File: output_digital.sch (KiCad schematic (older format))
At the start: 18 parts

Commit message: Primer version
Esquematico completo, faltan notas del revisor.
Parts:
- removed D? (x2): LED_ALT, symbol LED_ALT
- removed D?: DIODE, symbol DIODE
- removed J? (x2): Screw_Terminal_1x02, symbol Screw_Terminal_1x02
- removed K? (x4): RELAY-DPDT-EE2-SPLIT, symbol RELAY-DPDT-EE2-SPLIT
- removed Q? (x2): BT3904, TO_SOT_Packages_SMD:SOT-23, symbol MBT3904DW1
- removed R? (x3): 1k, symbol R
- removed R? (x2): 10k, symbol R
- added D1, D2, D5: LED_ALT, footprints:LED-0805, symbol LED_ALT
- added D4: MRA4003T3G, footprints:DO-214AA(SMB), symbol DIODE
- added J4, J5, J6: Screw_Terminal_1x02, footprints:TerminalBlock_Pheonix_MKDS1.5-2pol, symbol Screw_Terminal_1x02
- added Q1, Q2: MMBT3904, footprints:SOT23GDS, symbol MMBT3904
- added R3, R4, R5, R6: 1k, footprints:R_1206_HandSoldering, symbol R
- added R7, R8: 10k, footprints:R_1206_HandSoldering, symbol R
- added R9: 100, footprints:R_1206_HandSoldering, symbol R
- added U5, U6: G2RL-1A-E, footprints:Relay_SPST_Schrack-RP-II-1_RM3-5mm, symbol G5LE-1A-5DC
- D3: renamed from D?; value DIODE -> MRA4003T3G; footprint (none) -> footprints:DO-214AA(SMB); Description (none) -> Diode Standard 300V 1A SMA; Digikey# (none) -> MRA4003T3GOSTR-ND; Manf (none) -> ON Semiconductor; Manf# (none) -> MRA4003T3G; Mouser# (none) -> Value
- R2: renamed from R?; footprint (none) -> footprints:R_1206_HandSoldering; Description (none) -> 1k Ohm ±1% 0.25W, 1/4W Chip Resistor 1206 (3216 Metric) Moi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; Digikey# Value -> 311-1.00KFRTR-ND; Manf Value -> Yageo; Manf# Value -> RC1206FR-071KL; Mouser# (none) -> Value
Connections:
- net labels added: REL1_SEL, REL2_SEL, SSR_SEL
- wire segments 34 -> 39
- no-connect marks 2 -> 0
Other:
- note added: "Salida SSR (Solid State Realy)"
- note added: "Salidas a Relay - 16A - 440VAC, 300VDC"
- moved on the sheet: D3, R2

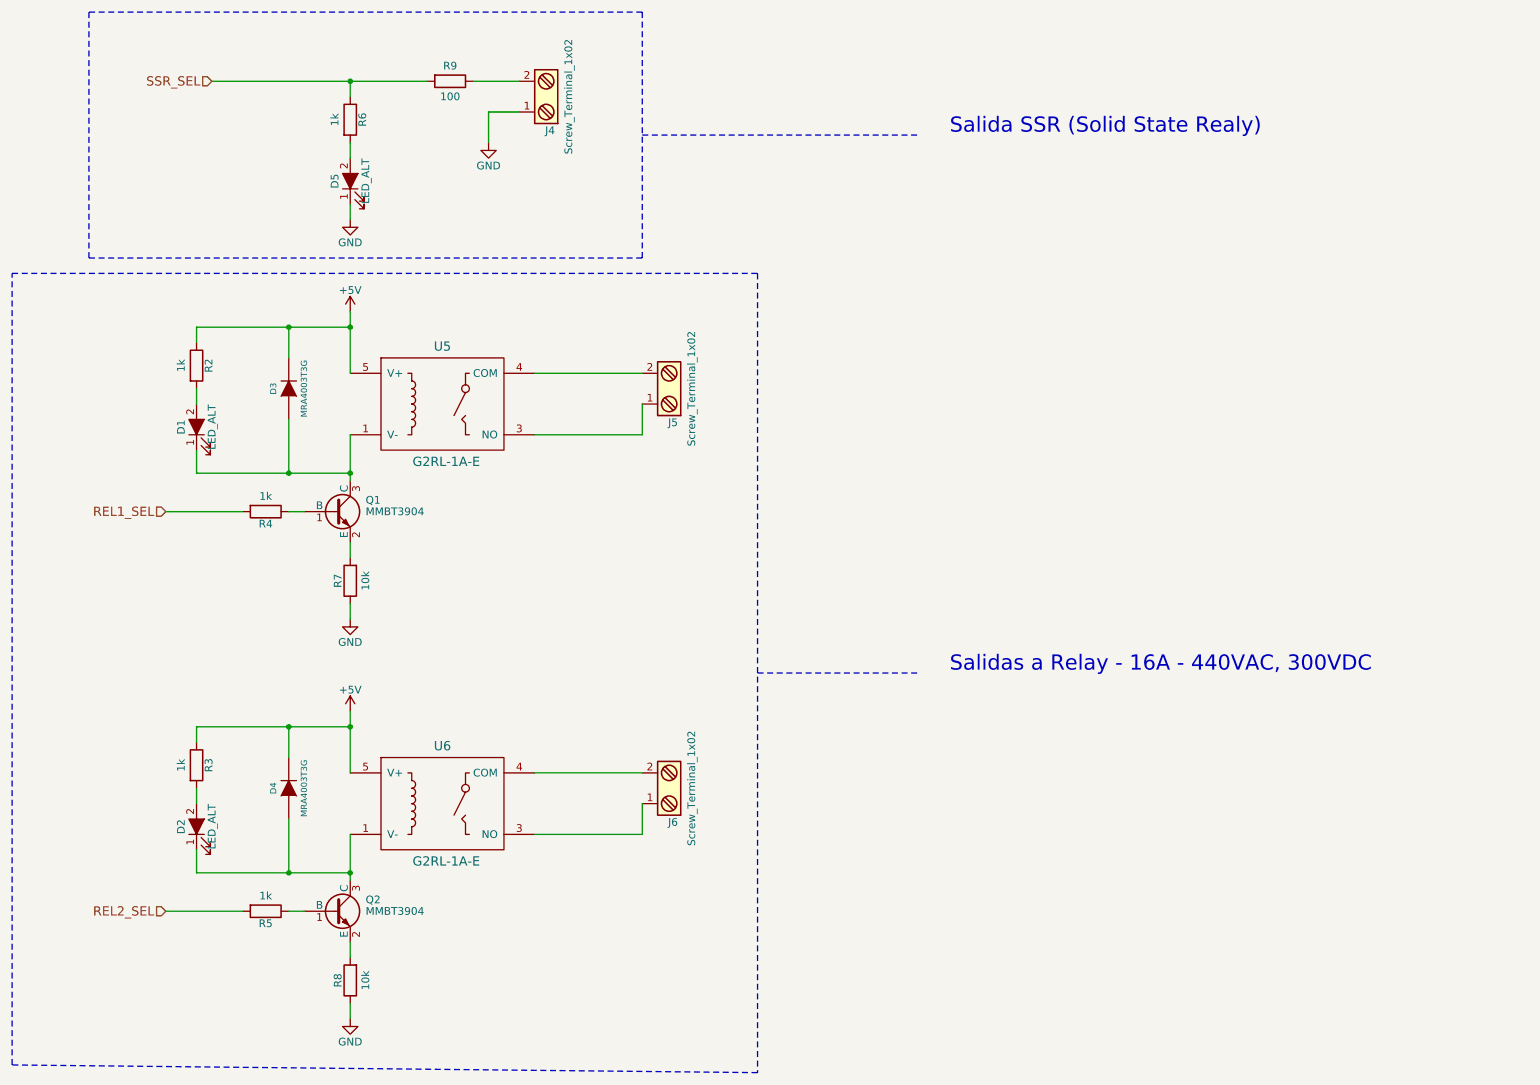
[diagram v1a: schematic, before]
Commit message: Primer revision
Se agregar correcciones del revisor. Se modifica entrada termocupla.
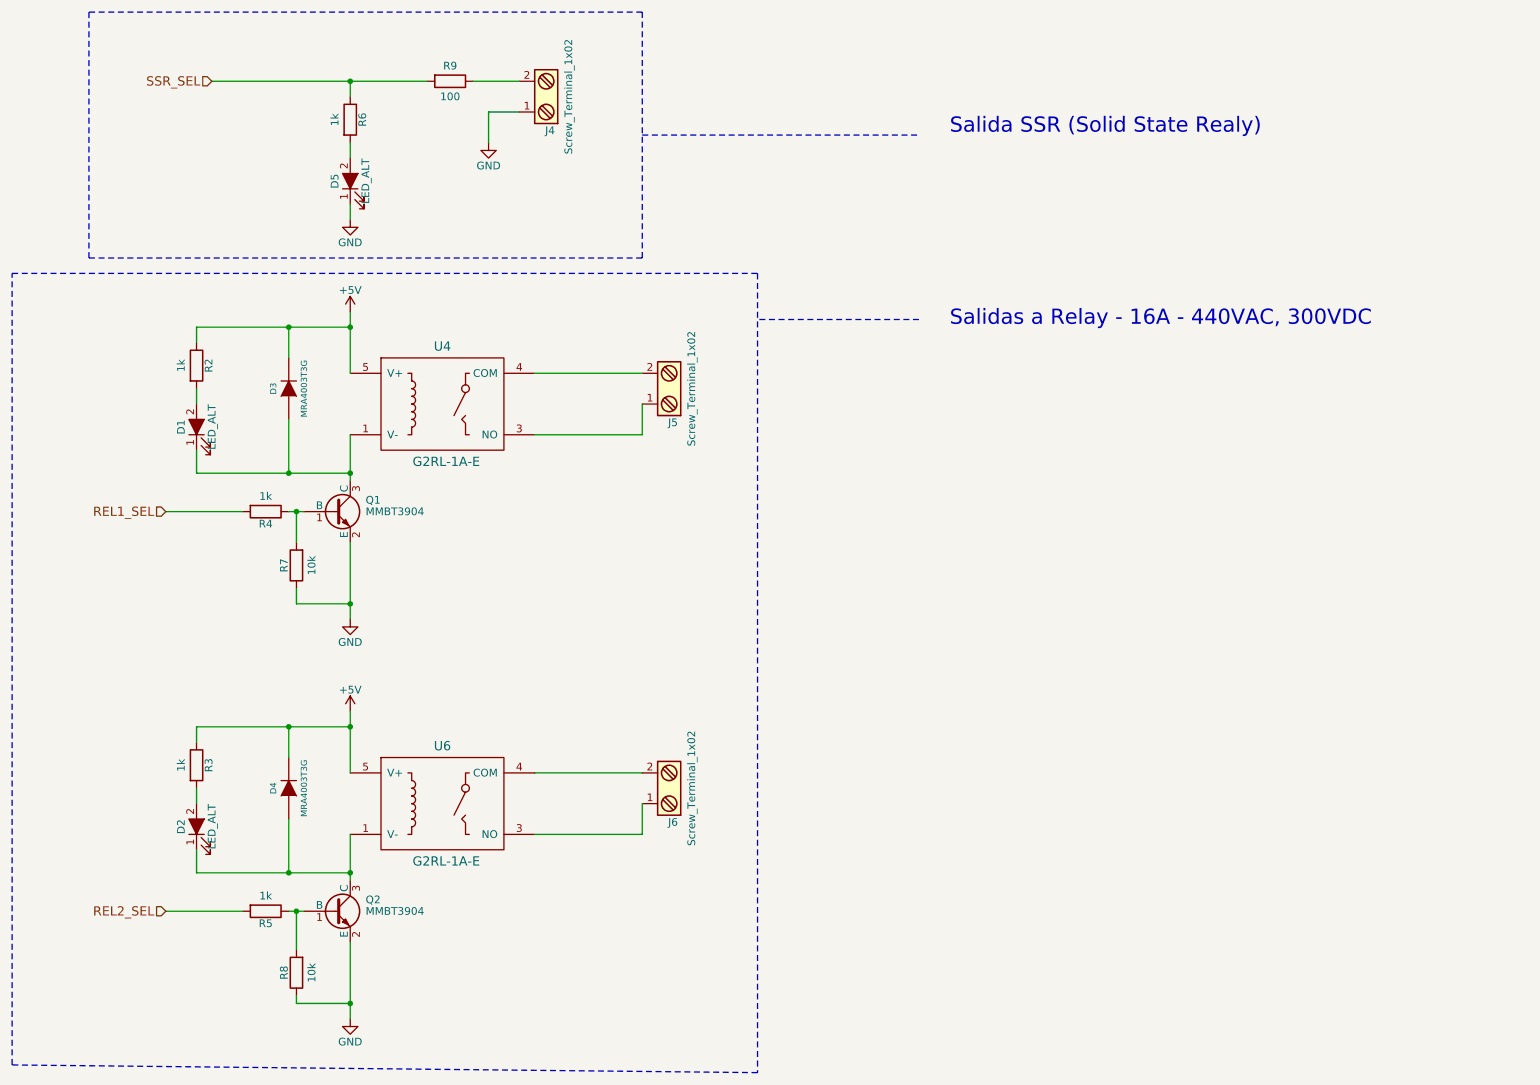
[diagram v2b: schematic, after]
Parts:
- removed U5: G2RL-1A-E, footprints:Relay_SPST_Schrack-RP-II-1_RM3-5mm, symbol G5LE-1A-5DC
- added U4: G2RL-1A-E, footprints:Relay_SPST_Schrack-RP-II-1_RM3-5mm, symbol G5LE-1A-5DC
- U6: Description General Purpose Relays 1 form A w/ TV3 24VDC Coil, 16A -> General Purpose Relays 1 form A w/ TV3 5VDC Coil, 16A; Manf# G2RL-1A-E-ASI DC24 -> G2RL-1A-E-ASI DC5; Mouser# 653-G2RL1AEASIDC24 -> 653-G2RL1AEASIDC5
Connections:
- net +5V: now also U4.5 (V+)
- net GND: now also Q1.2 (E), Q2.2 (E)
- net at D1.1 (K), D3.1 (A), Q1.3 (C): now also U4.1 (V-)
- net at Q1.1 (B), R4.1: now also R7.2
- net at J5.1: now also U4.3 (NO)
- net at J5.2: now also U4.4 (COM)
- net at Q2.1 (B), R5.1: now also R8.2
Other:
- moved on the sheet: R7, R8
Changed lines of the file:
@@
 EESchema Schematic File Version 2
-LIBS:tempRalayPoncho-rescue
-LIBS:power
-LIBS:device
-LIBS:transistors
-LIBS:conn
-LIBS:linear
-LIBS:regul
-LIBS:74xx
-LIBS:cmos4000
-LIBS:adc-dac
-LIBS:memory
-LIBS:xilinx
-LIBS:microcontrollers
-LIBS:dsp
-LIBS:microchip
-LIBS:analog_switches
-LIBS:motorola
-LIBS:texas
-LIBS:intel
-LIBS:audio
-LIBS:interface
-LIBS:digital-audio
-LIBS:philips
-LIBS:display
-LIBS:cypress
-LIBS:siliconi
-LIBS:opto
-LIBS:atmel
-LIBS:contrib
-LIBS:valves
-LIBS:ej2cese
-LIBS:analog-cache
-LIBS:ciaa-nxp-cache
-LIBS:relay
-LIBS:cmos_ieee
-LIBS:tempRalayPoncho-cache
+LIBS:TempRelay
+LIBS:tempRelayPoncho-cache
 EELAYER 25 0
 EELAYER END
@@
 encoding utf-8
 Sheet 4 4
-Title "Poncho Edu CIAA - Sensor Temperatura y Salidas digitales"
+Title "Poncho Edu CIAA - Salidas digitales"
 Date "2017-06-14"
 Rev "1.0"
-Comp "Autor: Francisco Suarez"
+Comp "Autor: Francisco Suárez"
 Comment1 "Revisor:  Mariano Orlante"
 Comment2 "Licencia: 'Docs/Licencia.txt\""
@@
 $EndComp
 $Comp
-L +5V #PWR018
+L +5V #PWR15
 U 1 1 5949AA7B
 P 3900 2550
-F 0 "#PWR018" H 3900 2400 50  0001 C CNN
+F 0 "#PWR15" H 3900 2400 50  0001 C CNN
 F 1 "+5V" H 3900 2690 50  0000 C CNN
 F 2 "" H 3900 2550 50  0001 C CNN
@@
 $EndComp
 $Comp
-L GND #PWR019
+L GND #PWR16
 U 1 1 5949AA9F
 P 3900 4550
-F 0 "#PWR019" H 3900 4300 50  0001 C CNN
+F 0 "#PWR16" H 3900 4300 50  0001 C CNN
 F 1 "GND" H 3900 4400 50  0000 C CNN
 F 2 "" H 3900 4550 50  0001 C CNN
@@
 	3600 3850 3500 3850
 Wire Wire Line
-	3900 4050 3900 4150
-Wire Wire Line
-	3900 4450 3900 4550
+	3900 4050 3900 4550
 Wire Wire Line
 	3200 3850 2700 3850
@@
 	5100 2950 5800 2950
 $Comp
-L +5V #PWR020
+L +5V #PWR17
 U 1 1 594AF973
 P 3900 5150
-F 0 "#PWR020" H 3900 5000 50  0001 C CNN
+F 0 "#PWR17" H 3900 5000 50  0001 C CNN
 F 1 "+5V" H 3900 5290 50  0000 C CNN
 F 2 "" H 3900 5150 50  0001 C CNN
@@
 $EndComp
 $Comp
-L GND #PWR021
+L GND #PWR18
 U 1 1 594AF979
 P 3900 7150
-F 0 "#PWR021" H 3900 6900 50  0001 C CNN
+F 0 "#PWR18" H 3900 6900 50  0001 C CNN
 F 1 "GND" H 3900 7000 50  0000 C CNN
 F 2 "" H 3900 7150 50  0001 C CNN
@@
 	3600 6450 3500 6450
 Wire Wire Line
-	3900 6650 3900 6750
-Wire Wire Line
-	3900 7050 3900 7150
+	3900 6650 3900 7150
 Wire Wire Line
 	3200 6450 2700 6450
@@
 	3900 1850 3900 1950
 $Comp
-L GND #PWR022
+L GND #PWR14
 U 1 1 594DE1D3
 P 3900 1950
-F 0 "#PWR022" H 3900 1700 50  0001 C CNN
+F 0 "#PWR14" H 3900 1700 50  0001 C CNN
 F 1 "GND" H 3900 1800 50  0000 C CNN
 F 2 "" H 3900 1950 50  0001 C CNN
@@
 $EndComp
 $Comp
-L GND #PWR023
+L GND #PWR19
 U 1 1 594DE220
 P 4800 1450
-F 0 "#PWR023" H 4800 1200 50  0001 C CNN
+F 0 "#PWR19" H 4800 1200 50  0001 C CNN
 F 1 "GND" H 4800 1300 50  0000 C CNN
 F 2 "" H 4800 1450 50  0001 C CNN
@@
 Text HLabel 2700 6450 0    60   Input ~ 0
 REL2_SEL
-$Comp
-L G5LE-1A-5DC U5
-U 1 1 594F9275
-P 4500 3150
-F 0 "U5" H 4500 3525 60  0000 C CNN
-F 1 "G2RL-1A-E" H 4525 2775 60  0000 C CNN
-F 2 "footprints:Relay_SPST_Schrack-RP-II-1_RM3-5mm" H 4500 3150 60  0001 C CNN
-F 3 "en-g2rl-472571.pdf" H 4500 3150 60  0001 C CNN
-F 4 "Omron Electronics" H 4500 3150 60  0001 C CNN "Manf"
-F 5 "G2RL-1A-E-ASI DC24" H 4500 3150 60  0001 C CNN "Manf#"
-F 6 "Value" H 4500 3150 60  0001 C CNN "Digikey#"
-F 7 "653-G2RL1AEASIDC24" H 4500 3150 60  0001 C CNN "Mouser#"
-F 8 "General Purpose Relays 1 form A w/ TV3 24VDC Coil, 16A" H 4500 3150 60  0001 C CNN "Description"
-	1    4500 3150
-	1    0    0    -1
-$EndComp
 Wire Wire Line
 	3900 3650 3900 3350
@@
 L R R7
 U 1 1 594F5EE4
-P 3900 4300
-F 0 "R7" V 3980 4300 50  0000 C CNN
-F 1 "10k" V 3800 4300 50  0000 C CNN
-F 2 "footprints:R_1206_HandSoldering" V 3830 4300 50  0001 C CNN
-F 3 "../Datasheets/PYu-RC_Group_51_RoHS_L_7.pdf" H 3900 4300 50  0001 C CNN
-F 4 "Yageo" H 3900 4300 60  0001 C CNN "Manf"
-F 5 "RC1206JR-0710KL" H 3900 4300 60  0001 C CNN "Manf#"
-F 6 "311-10KERTR-ND" H 3900 4300 60  0001 C CNN "Digikey#"
-F 7 "Value" H 3900 4300 60  0001 C CNN "Mouser#"
-F 8 "10k Ohm ±5% 0.25W, 1/4W Chip, Moisture Resistant Thick Film" H 3900 4300 60  0001 C CNN "Description"
-	1    3900 4300
+P 3550 4200
+F 0 "R7" V 3630 4200 50  0000 C CNN
+F 1 "10k" V 3450 4200 50  0000 C CNN
+F 2 "footprints:R_1206_HandSoldering" V 3480 4200 50  0001 C CNN
+F 3 "../Datasheets/PYu-RC_Group_51_RoHS_L_7.pdf" H 3550 4200 50  0001 C CNN
+F 4 "Yageo" H 3550 4200 60  0001 C CNN "Manf"
+F 5 "RC1206JR-0710KL" H 3550 4200 60  0001 C CNN "Manf#"
+F 6 "311-10KERTR-ND" H 3550 4200 60  0001 C CNN "Digikey#"
+F 7 "Value" H 3550 4200 60  0001 C CNN "Mouser#"
+F 8 "10k Ohm ±5% 0.25W, 1/4W Chip, Moisture Resistant Thick Film" H 3550 4200 60  0001 C CNN "Description"
+	1    3550 4200
 	-1   0    0    1
 $EndComp
@@
 L R R8
 U 1 1 594F7CE0
-P 3900 6900
-F 0 "R8" V 3980 6900 50  0000 C CNN
-F 1 "10k" V 3800 6900 50  0000 C CNN
-F 2 "footprints:R_1206_HandSoldering" V 3830 6900 50  0001 C CNN
-F 3 "../Datasheets/PYu-RC_Group_51_RoHS_L_7.pdf" H 3900 6900 50  0001 C CNN
-F 4 "Yageo" H 3900 6900 60  0001 C CNN "Manf"
-F 5 "RC1206JR-0710KL" H 3900 6900 60  0001 C CNN "Manf#"
-F 6 "311-10KERTR-ND" H 3900 6900 60  0001 C CNN "Digikey#"
-F 7 "Value" H 3900 6900 60  0001 C CNN "Mouser#"
-F 8 "10k Ohm ±5% 0.25W, 1/4W Chip, Moisture Resistant Thick Film" H 3900 6900 60  0001 C CNN "Description"
-	1    3900 6900
+P 3550 6850
+F 0 "R8" V 3630 6850 50  0000 C CNN
+F 1 "10k" V 3450 6850 50  0000 C CNN
+F 2 "footprints:R_1206_HandSoldering" V 3480 6850 50  0001 C CNN
+F 3 "../Datasheets/PYu-RC_Group_51_RoHS_L_7.pdf" H 3550 6850 50  0001 C CNN
+F 4 "Yageo" H 3550 6850 60  0001 C CNN "Manf"
+F 5 "RC1206JR-0710KL" H 3550 6850 60  0001 C CNN "Manf#"
+F 6 "311-10KERTR-ND" H 3550 6850 60  0001 C CNN "Digikey#"
+F 7 "Value" H 3550 6850 60  0001 C CNN "Mouser#"
+F 8 "10k Ohm ±5% 0.25W, 1/4W Chip, Moisture Resistant Thick Film" H 3550 6850 60  0001 C CNN "Description"
+	1    3550 6850
 	-1   0    0    1
 $EndComp
@@
 F 3 "en-g2rl-472571.pdf" H 4500 5750 60  0001 C CNN
 F 4 "Omron Electronics" H 4500 5750 60  0001 C CNN "Manf"
-F 5 "G2RL-1A-E-ASI DC24" H 4500 5750 60  0001 C CNN "Manf#"
+F 5 "G2RL-1A-E-ASI DC5" H 4500 5750 60  0001 C CNN "Manf#"
 F 6 "Value" H 4500 5750 60  0001 C CNN "Digikey#"
-F 7 "653-G2RL1AEASIDC24" H 4500 5750 60  0001 C CNN "Mouser#"
-F 8 "General Purpose Relays 1 form A w/ TV3 24VDC Coil, 16A" H 4500 5750 60  0001 C CNN "Description"
+F 7 "653-G2RL1AEASIDC5" H 4500 5750 60  0001 C CNN "Mouser#"
+F 8 "General Purpose Relays 1 form A w/ TV3 5VDC Coil, 16A" H 4500 5750 60  0001 C CNN "Description"
 	1    4500 5750
 	1    0    0    -1
@@
 Wire Notes Line
 	5800 1400 7600 1400
-Wire Notes Line
-	6550 4900 7600 4900
 Text Notes 7800 1400 0    99   ~ 0
 Salida SSR (Solid State Realy)
-Text Notes 7800 4900 0    99   ~ 0
+Text Notes 7800 2650 0    99   ~ 0
 Salidas a Relay - 16A - 440VAC, 300VDC
+Wire Wire Line
+	3550 4050 3550 3850
+Connection ~ 3550 3850
+Wire Wire Line
+	3550 4350 3550 4450
+Wire Wire Line
+	3550 4450 3900 4450
+Connection ~ 3900 4450
+Wire Wire Line
+	3550 6700 3550 6450
+Connection ~ 3550 6450
+Wire Wire Line
+	3900 7050 3550 7050
+Wire Wire Line
+	3550 7050 3550 7000
+Connection ~ 3900 7050
+$Comp
+L G5LE-1A-5DC U4
+U 1 1 59510F67
+P 4500 3150
+F 0 "U4" H 4500 3525 60  0000 C CNN
+F 1 "G2RL-1A-E" H 4525 2775 60  0000 C CNN
+F 2 "footprints:Relay_SPST_Schrack-RP-II-1_RM3-5mm" H 4500 3150 60  0001 C CNN
+F 3 "en-g2rl-472571.pdf" H 4500 3150 60  0001 C CNN
+F 4 "Omron Electronics" H 4500 3150 60  0001 C CNN "Manf"
+F 5 "G2RL-1A-E-ASI DC5" H 4500 3150 60  0001 C CNN "Manf#"
+F 6 "Value" H 4500 3150 60  0001 C CNN "Digikey#"
+F 7 "653-G2RL1AEASIDC5" H 4500 3150 60  0001 C CNN "Mouser#"
+F 8 "General Purpose Relays 1 form A w/ TV3 5VDC Coil, 16A" H 4500 3150 60  0001 C CNN "Description"
+	1    4500 3150
+	1    0    0    -1
+$EndComp
+Wire Notes Line
+	7600 2600 6550 2600
 $EndSCHEMATC
